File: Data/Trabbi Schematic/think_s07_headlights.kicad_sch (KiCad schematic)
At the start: 12 parts, among them K1 DRL Relay R5, K2 Park Light Relay R17, SW1 Headlight Switch (C25)

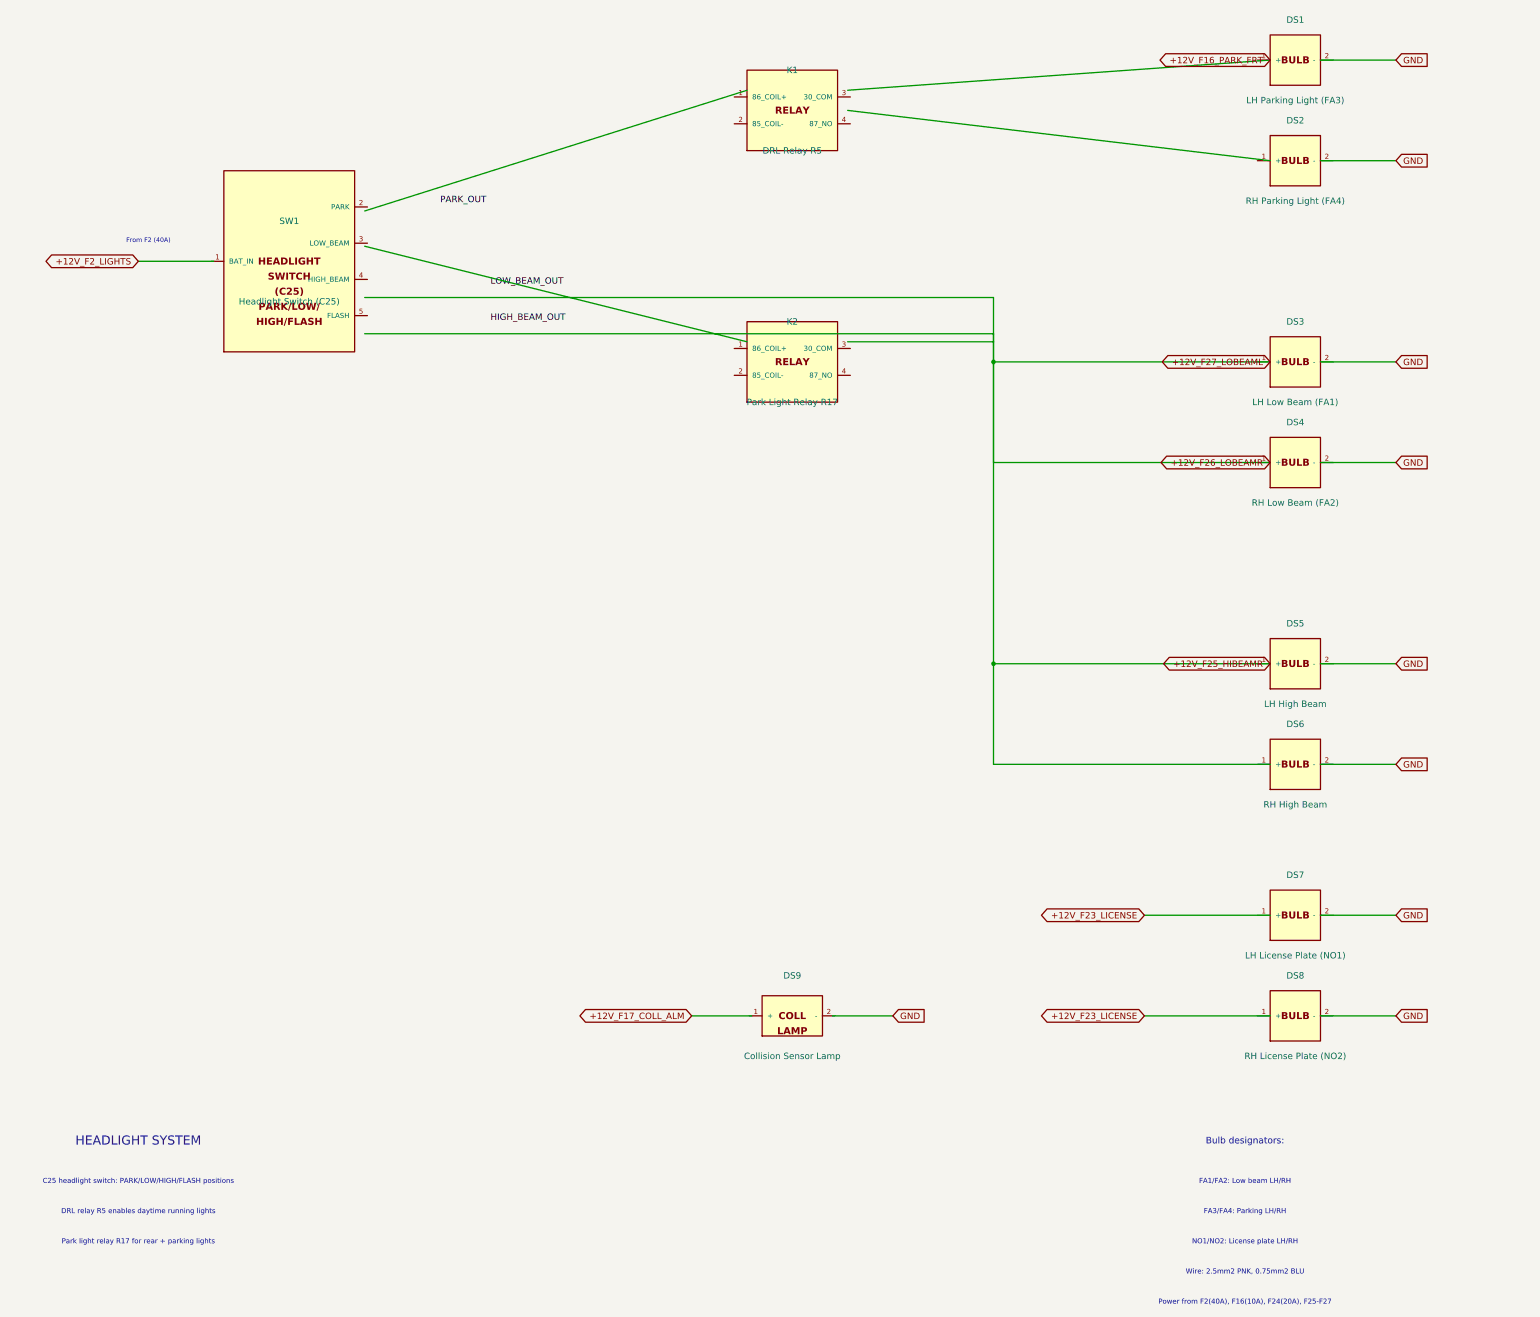
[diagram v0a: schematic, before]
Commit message: Fix wire-to-pin connections: use exact calculated pin positions
Refactored gen_think_complete.py to compute exact pin schematic
coordinates instead of using approximate manual offsets. Added p()
method to Sheet class that transforms symbol-local pin positions to
schematic coordinates. All 232 wire calls across 13 sub-sheet
generators now use p() for pin endpoints, fixing misaligned
connections (previously off by 0.54-10+ units).

Co-Authored-By: Claude Opus 4.6 <noreply@anthropic.com>
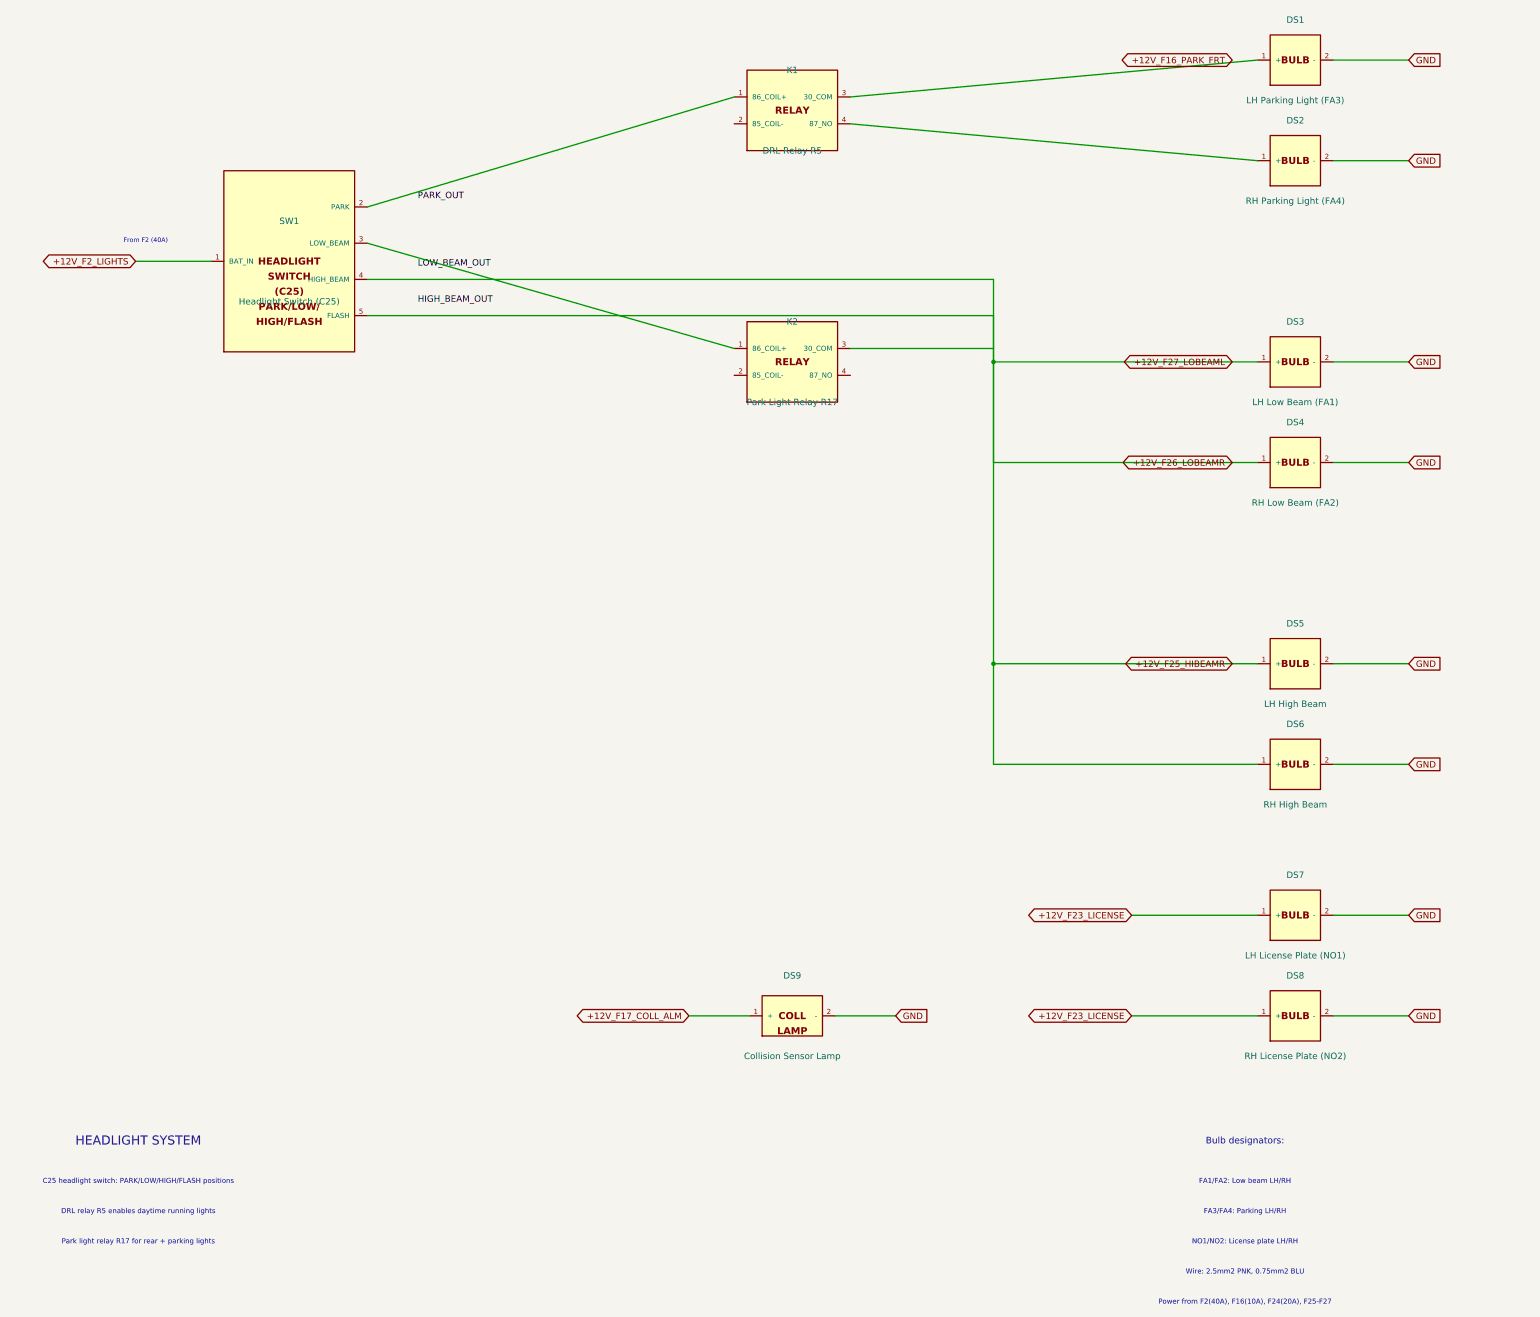
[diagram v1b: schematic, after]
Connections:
- net +12V_F17_COLL_ALM: now also DS9.1 (+)
- net +12V_F23_LICENSE: now also DS7.1 (+), DS8.1 (+)
- net +12V_F25_HIBEAMR: now also DS3.1 (+), DS4.1 (+), DS5.1 (+), DS6.1 (+), SW1.4 (HIGH_BEAM), SW1.5 (FLASH)
- net +12V_F2_LIGHTS: now also SW1.1 (BAT_IN)
- net GND: now also DS1.2 (-), DS2.2 (-), DS3.2 (-), DS4.2 (-), DS5.2 (-), DS6.2 (-), DS7.2 (-), DS8.2 (-), DS9.2 (-)
- net at DS2.1 (+): now also K1.4 (87_NO)
- net at K2.1 (86_COIL+): now also SW1.3 (LOW_BEAM)
- net at DS1.1 (+): now also K1.3 (30_COM)
- net at K1.1 (86_COIL+): now also SW1.2 (PARK)

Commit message: Enforce orthogonal routing and 1.27mm grid alignment
- Add _g() grid snap function to Sheet class (rounds all coordinates to nearest 1.27mm)
- Add wire_l() method for L-shaped orthogonal routing (horizontal+vertical segments)
- Apply grid snapping in p(), place(), wire(), label(), glabel(), junction(), no_connect(), defsym()
- Replace all 19 diagonal wire calls with wire_l() across S02, S06, S07, S08, S10, S12, S13
- All wire segments now strictly horizontal or vertical, no diagonals
- All coordinates verified on 1.27mm (50mil) KiCad standard grid

Co-Authored-By: Claude Opus 4.6 <noreply@anthropic.com>
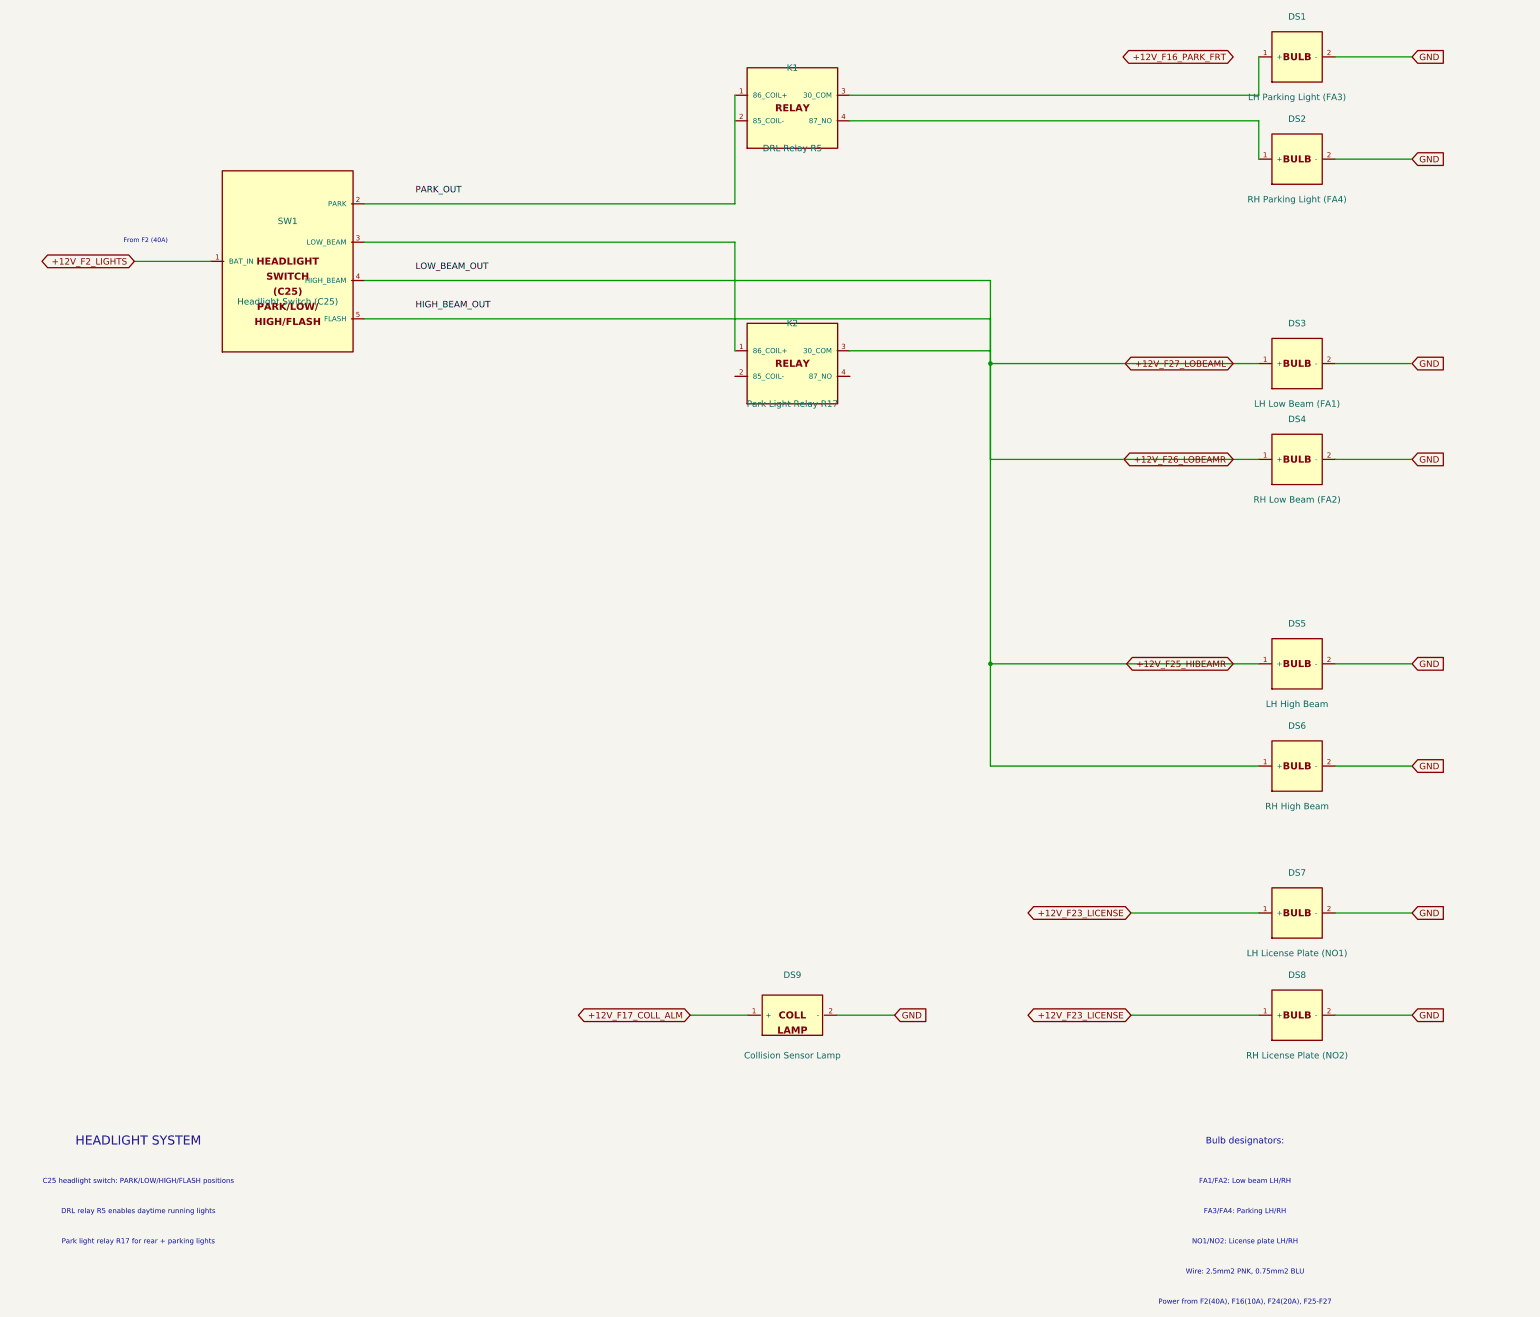
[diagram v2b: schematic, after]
